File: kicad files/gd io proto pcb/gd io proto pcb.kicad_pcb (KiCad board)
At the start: 2 copper layers, 94.8 x 64.6 mm, 39 parts, among them J1 Pwr, J10 DEV LA, J11 Annunciate, J12 Apple_II_Slot, J13 Slot Maker, J14 Slot Maker LA, J15 Slot-Only Sigs, J16 IO Selector, J17 -5V, J18 IOSEL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

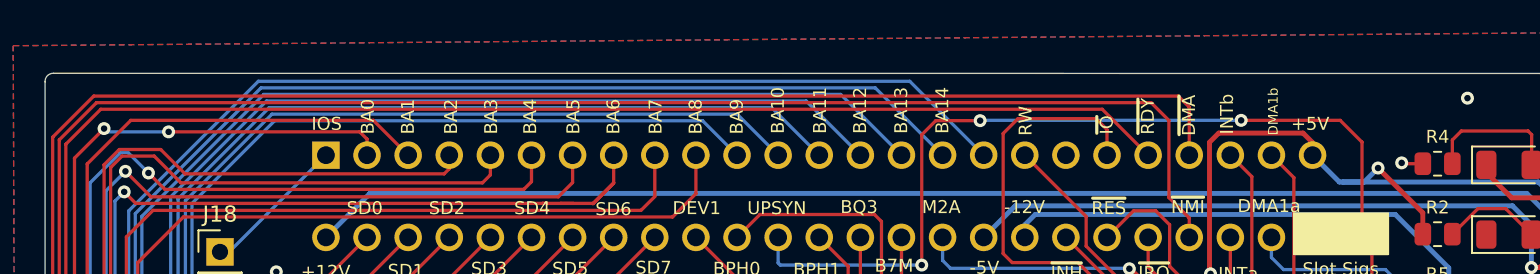
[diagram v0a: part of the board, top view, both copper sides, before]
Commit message: added text to mark front/back of "IIe"
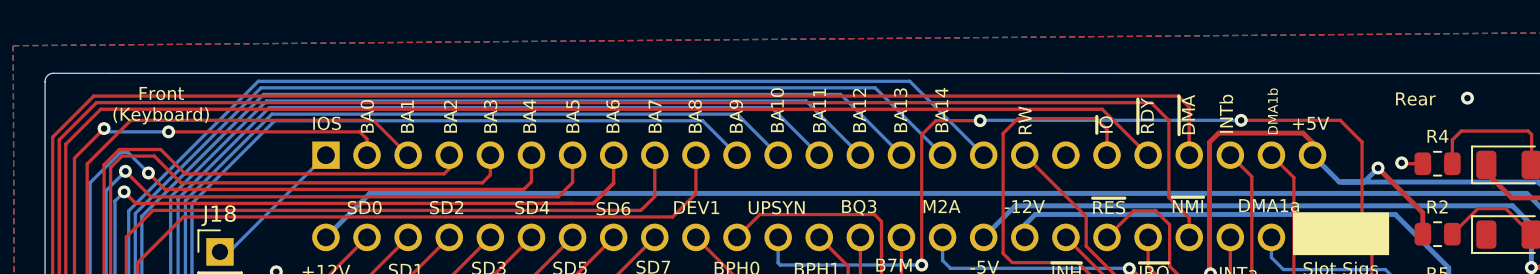
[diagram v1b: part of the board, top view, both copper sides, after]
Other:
- board text added: "Front (Keyboard)"
- board text added: "Rear"

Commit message: mk2 initial - kicad 7 upgrade
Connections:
- net /~C038 renamed /~{C038}
- net /~DEV1 renamed /~{DEV1}
- net /~DEV2 renamed /~{DEV2}
- net /~DEV3 renamed /~{DEV3}
- net /~DEV4 renamed /~{DEV4}
- net /~DEV5 renamed /~{DEV5}
- net /~DEV6 renamed /~{DEV6}
- net /~DEV7 renamed /~{DEV7}
- net /~DMA renamed /~{DMA}
- net /~EN245 renamed /~{EN245}
- net /~INH renamed /~{INH}
- net /~INTDEV1 renamed /~{INTDEV1}
- net /~INTDEV2 renamed /~{INTDEV2}
- net /~INTDEV5 renamed /~{INTDEV5}
- net /~INTDEV6 renamed /~{INTDEV6}
- net /~INTDEV7 renamed /~{INTDEV7}
- net /~IOSEL renamed /~{IOSEL}
- net /~IOSEL1 renamed /~{IOSEL1}
- net /~IOSEL2 renamed /~{IOSEL2}
- net /~IOSEL3 renamed /~{IOSEL3}
- net /~IOSEL4 renamed /~{IOSEL4}
- net /~IOSEL5 renamed /~{IOSEL5}
- net /~IOSEL6 renamed /~{IOSEL6}
- net /~IOSEL7 renamed /~{IOSEL7}
- net /~IOSTRB renamed /~{IOSTRB}
- net /~IRQ renamed /~{IRQ}
- net /~NMI renamed /~{NMI}
- net /~RDY renamed /~{RDY}
- net /~RESET renamed /~{RESET}
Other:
- net class Default removed
- net class Power removed
- board text added: "~{C0}"
- board text added: "~{DMA}"
- board text added: "~{EN245}"
- board text added: "~{INH}"
- board text added: "~{INTD6}"
- board text added: "~{IOS}"
- board text added: "~{IO}"
- board text added: "~{IRQ}"
- board text added: "~{NMI}"
- board text added: "~{RDY}"
- board text added: "~{RES}"
- board text removed: "~C0"
- board text removed: "~DMA"
- board text removed: "~EN245"
- board text removed: "~INH"
- board text removed: "~INTD6"
- board text removed: "~IO"
- board text removed: "~IOS"
- board text removed: "~IRQ"
- board text removed: "~NMI"
- board text removed: "~RDY"
- board text removed: "~RES"

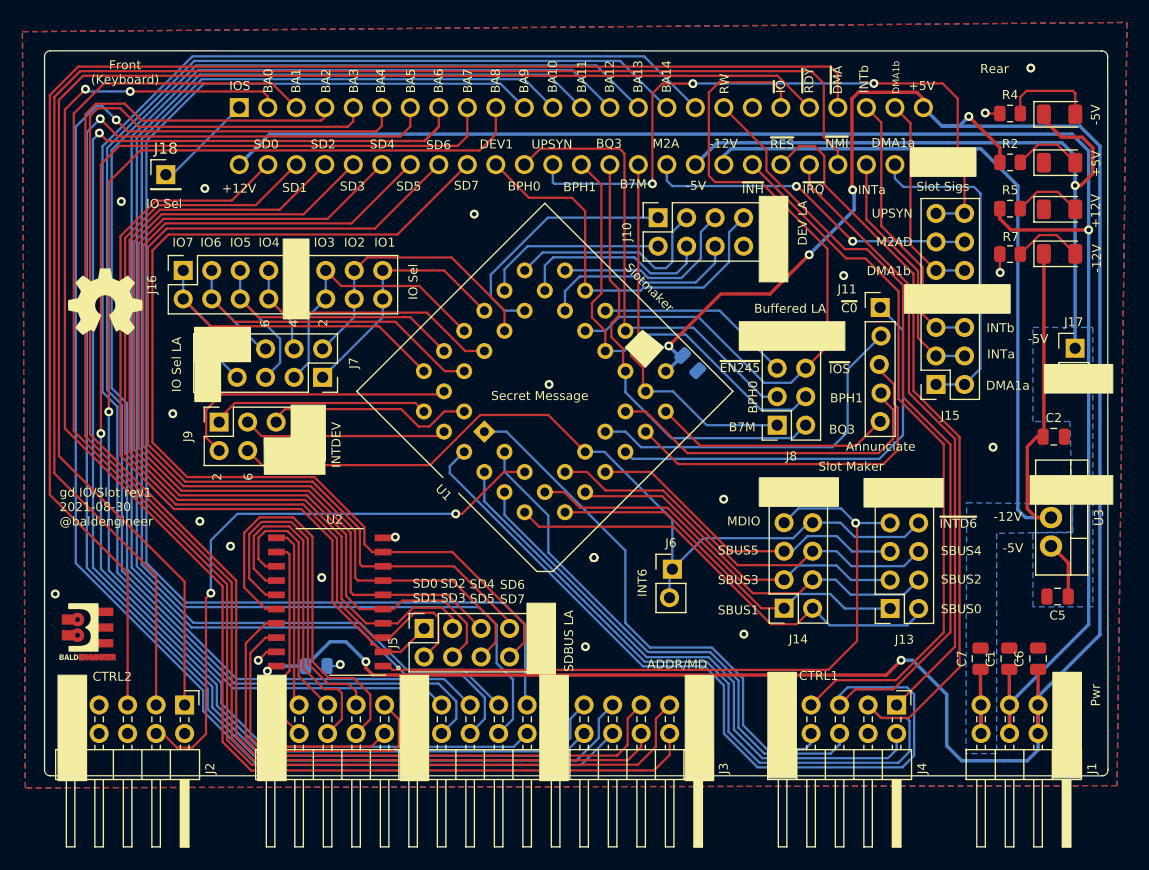
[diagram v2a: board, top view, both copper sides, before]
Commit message: resolves #57. now there is a 2-pin header for dev select (and a pin to probe with logic analyzer.) also fixed an issue with the 245 enable signal (whoops.)
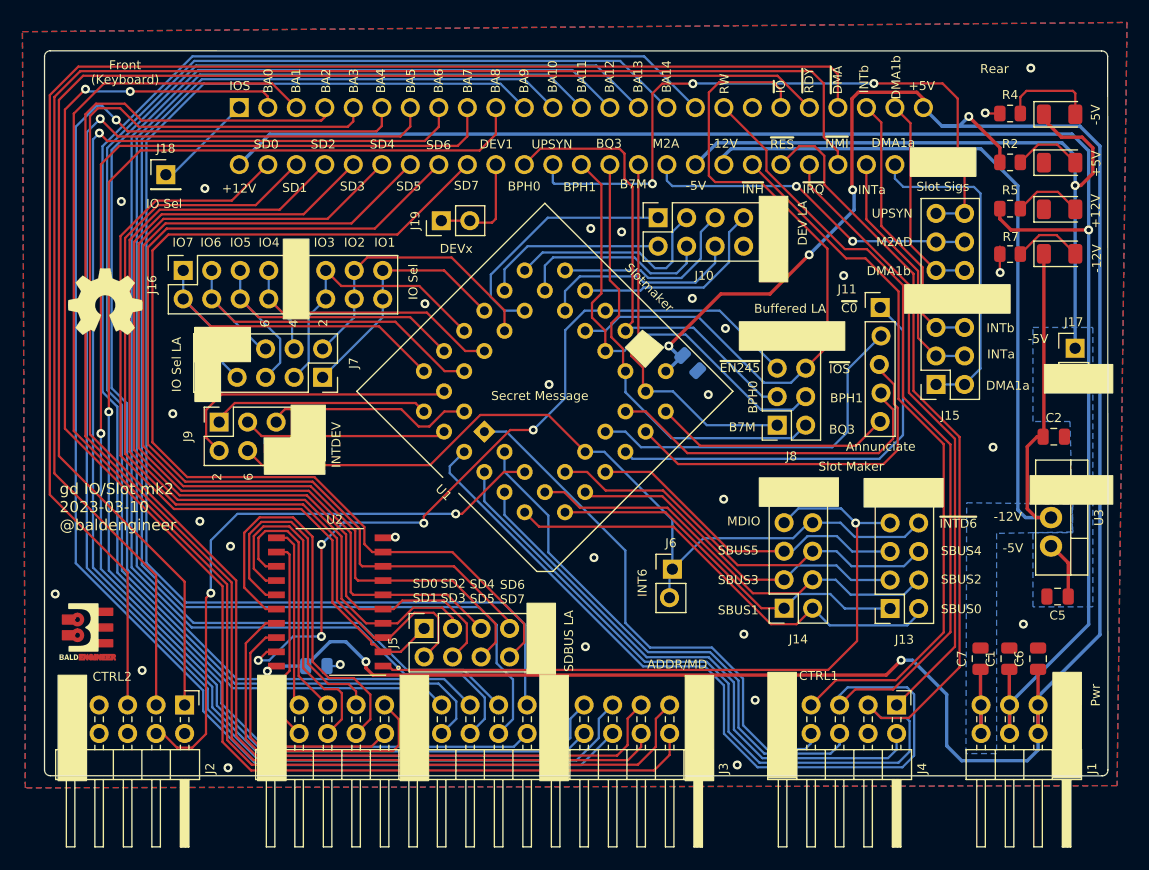
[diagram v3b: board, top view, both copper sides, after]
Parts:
- added J19: DEVx, Connector_PinHeader_2.54mm:PinHeader_1x02_P2.54mm_Vertical, F.Cu at (90.5, 137.2)
- U2: value 74HCT245-CHECK FOOTPRINT -> 74HCT245
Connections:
- J12 pad 19: Net-(J12-Pad19) -> unconnected-(J12-Pad19)
- J12 pad 41: /~{DEV1} -> /~{DEVx}
- J2 pad 2: Net-(J2-Pad2) -> unconnected-(J2-Pin_2-Pad2)
- J2 pad 6: Net-(J2-Pad6) -> unconnected-(J2-Pin_6-Pad6)
- J2 pad 7: Net-(J2-Pad7) -> unconnected-(J2-Pin_7-Pad7)
- J2 pad 8: Net-(J2-Pad8) -> unconnected-(J2-Pin_8-Pad8)
- J4 pad 4: Net-(J4-Pad4) -> unconnected-(J4-Pin_4-Pad4)
- U2 pad 19: /EN245 -> /~{EN245}
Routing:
- net /~{EN245}: track 17.4 -> 71.9 mm, vias 0 -> 5
- net /~{DEV1}: track 35.1 -> 18.4 mm
- net /~{DEVx}: track 0.00 -> 9.65 mm
- net /BA6: track 127.2 -> 124.3 mm
- net /EN245: track 1.93 -> 0.00 mm, vias 1 -> 0
- net +5V: track 209.8 -> 208.3 mm
- net /SBUS5: track 29.4 -> 28.7 mm
- net /~{INTDEV6}: track 75.8 -> 75.1 mm
- net /MD7: track 16.3 -> 15.7 mm
- net /KSEL0: track 53.4 -> 52.8 mm
- net /SDBUS1: track 80.3 -> 79.7 mm
- net /SDBUS6: track 87.7 -> 87.1 mm
- net /~{IOSEL}: track 9.02 -> 8.45 mm
- net /~{INTDEV5}: track 18.2 -> 17.6 mm
- net /SBUS3: track 31.5 -> 31.0 mm
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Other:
- board text added: "gd IO/Slot mk2 2023-03-10 @baldengineer"
- board text removed: "gd IO/Slot rev1 2021-08-30 @baldengineer"

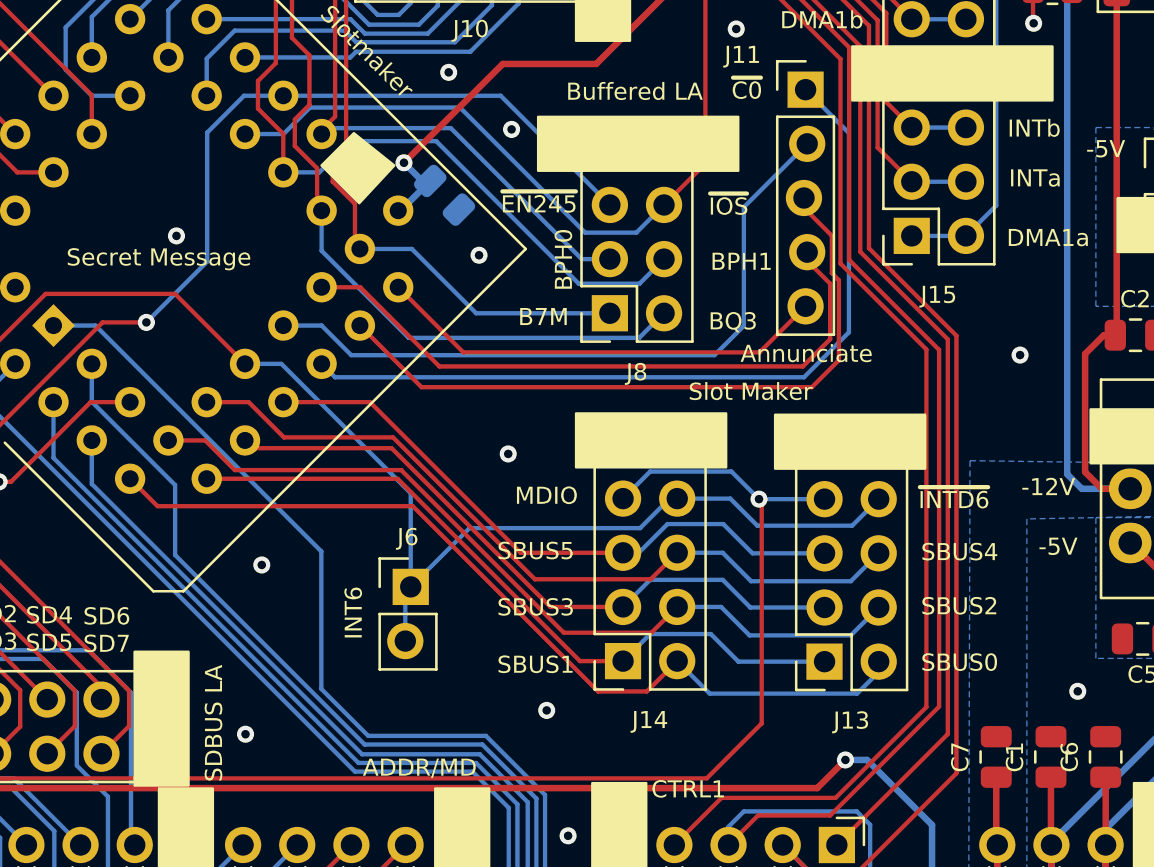
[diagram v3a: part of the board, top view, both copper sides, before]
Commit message: fixed sbus signals (#18)
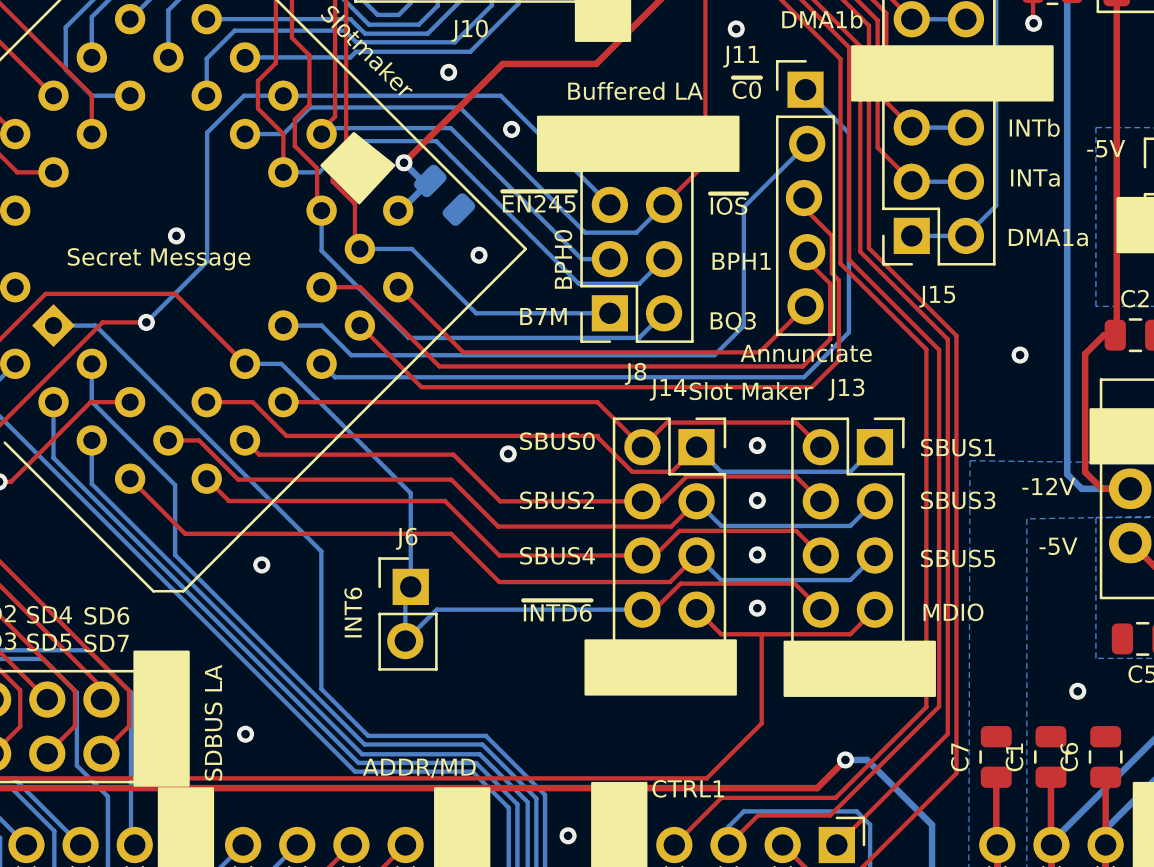
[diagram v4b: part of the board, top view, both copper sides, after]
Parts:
- moved J14 10.6 mm to (124.5, 161.7), turned to 0 degrees
- moved J13 10.3 mm to (132.8, 161.7), turned to 0 degrees
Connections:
- U1 pad 10: /SBUS4 -> /SBUS1
- U1 pad 11: /SBUS5 -> /SBUS0
- U1 pad 6: /SBUS0 -> /SBUS5
- U1 pad 7: /SBUS1 -> /SBUS4
- U1 pad 8: /SBUS2 -> /SBUS3
- U1 pad 9: /SBUS3 -> /SBUS2
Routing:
- net /SBUS0: track 40.9 -> 27.0 mm
- net /SBUS5: track 28.7 -> 38.4 mm
- net /SBUS2: track 38.6 -> 29.1 mm
- net /MDIN-OUT: track 64.0 -> 56.5 mm, vias 1 -> 0
- net /SBUS4: track 36.6 -> 30.7 mm
- net /SBUS3: track 31.0 -> 36.3 mm
- net /~{INTDEV6}: track 75.1 -> 71.3 mm
- net /SBUS1: track 33.6 -> 34.2 mm
- net GND: vias 29 -> 32
